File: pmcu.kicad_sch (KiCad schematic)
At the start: 1 part, among them U10 ATtiny44A-CC

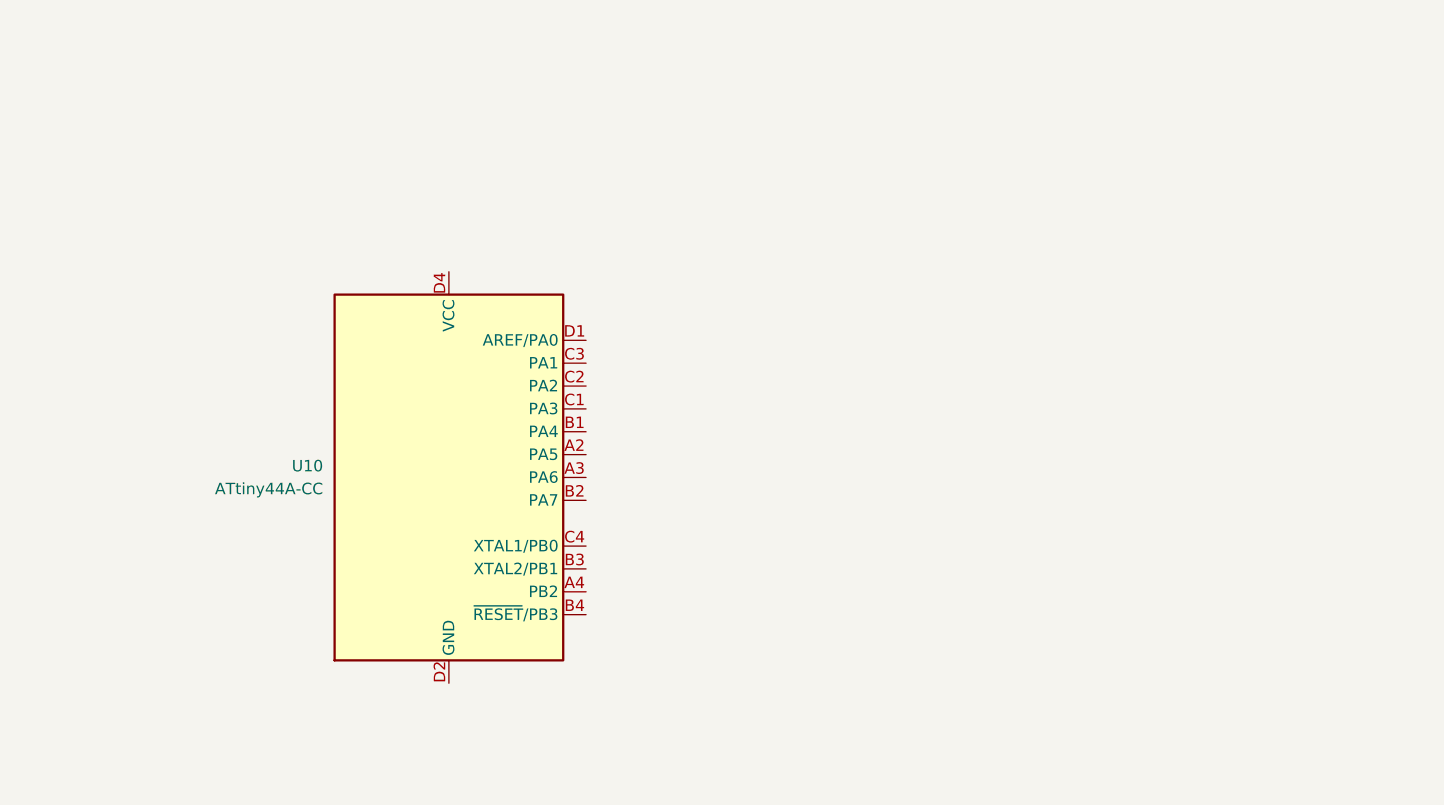
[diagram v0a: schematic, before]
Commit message: Added pMCU
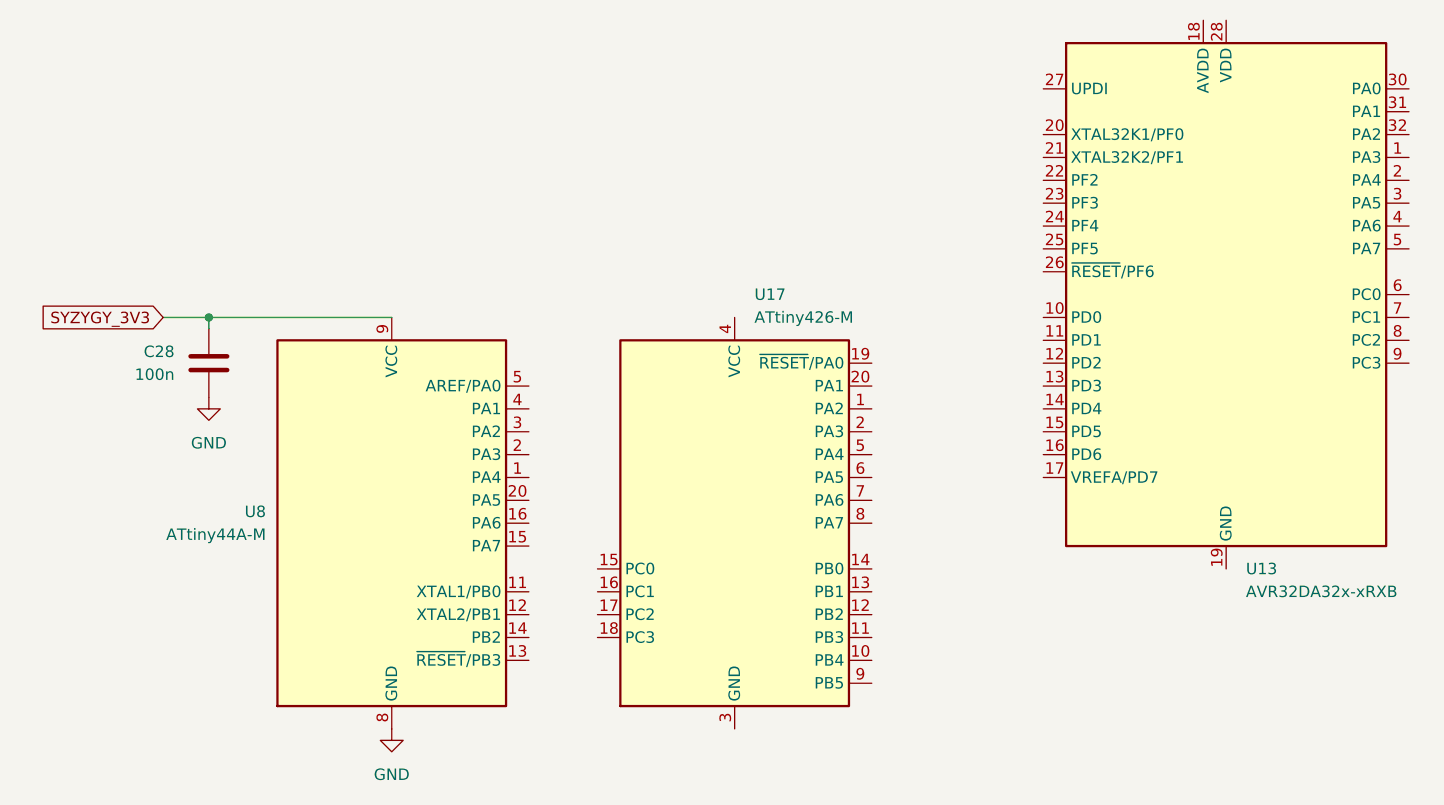
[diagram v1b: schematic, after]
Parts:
- removed U10: ATtiny44A-CC, Package_BGA:UFBGA-15_3.0x3.0mm_Layout4x4_P0.65mm, symbol MCU_Microchip_ATtiny:ATtiny44A-CC
- added C28: 100n, symbol Device:C
- added U13: AVR32DA32x-xRXB, Package_DFN_QFN:QFN-32-1EP_5x5mm_P0.5mm_EP3.1x3.1mm, symbol MCU_Microchip_AVR_Dx:AVR32DA32x-xRXB
- added U17: ATtiny426-M, Package_DFN_QFN:VQFN-20-1EP_3x3mm_P0.4mm_EP1.7x1.7mm, symbol MCU_Microchip_ATtiny:ATtiny426-M
- added U8: ATtiny44A-M, Package_DFN_QFN:QFN-20-1EP_4x4mm_P0.5mm_EP2.6x2.6mm, symbol MCU_Microchip_ATtiny:ATtiny44A-M
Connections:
- new net: U13.19 (GND), U13.29 (GND), U13.33 (GND)
- new net: U17.21 (GND), U17.3 (GND)
- new net GND: C28.2, U8.21 (GND), U8.8 (GND)
- new net SYZYGY_3V3: C28.1, U8.9 (VCC)
